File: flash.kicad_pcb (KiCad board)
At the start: 2 copper layers, 17.8 x 27.9 mm, 14 parts, among them J1 USB_B_Micro, J2 Conn_01x05, Q1 PN2222A, Q2 PN2222A, U1 CP2102N-A01-GQFN24

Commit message: Finish PCB
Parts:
- U1: footprint digikey-footprints:QFN-24-1EP_4x4mm -> Housings_DFN_QFN:QFN-24-1EP_4x4mm_Pitch0.5mm
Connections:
- R1 pad 1: Net-(R1-Pad1) -> Net-(C1-Pad1)
- U1 pad 5: Net-(R1-Pad1) -> Net-(C1-Pad1)
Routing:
- net Net-(C1-Pad1): track 7.98 -> 25.9 mm, vias 0 -> 2
- net Net-(R1-Pad1): track 16.7 -> 0.00 mm, vias 2 -> 0
- net GND: track 26.6 -> 30.4 mm, vias 5 -> 6
- net Net-(J1-Pad3): track 16.0 -> 15.3 mm
- net Net-(J1-Pad2): track 14.8 -> 14.2 mm
- net Net-(Q1-Pad1): track 16.0 -> 15.4 mm
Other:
- board text added: "v0.1"

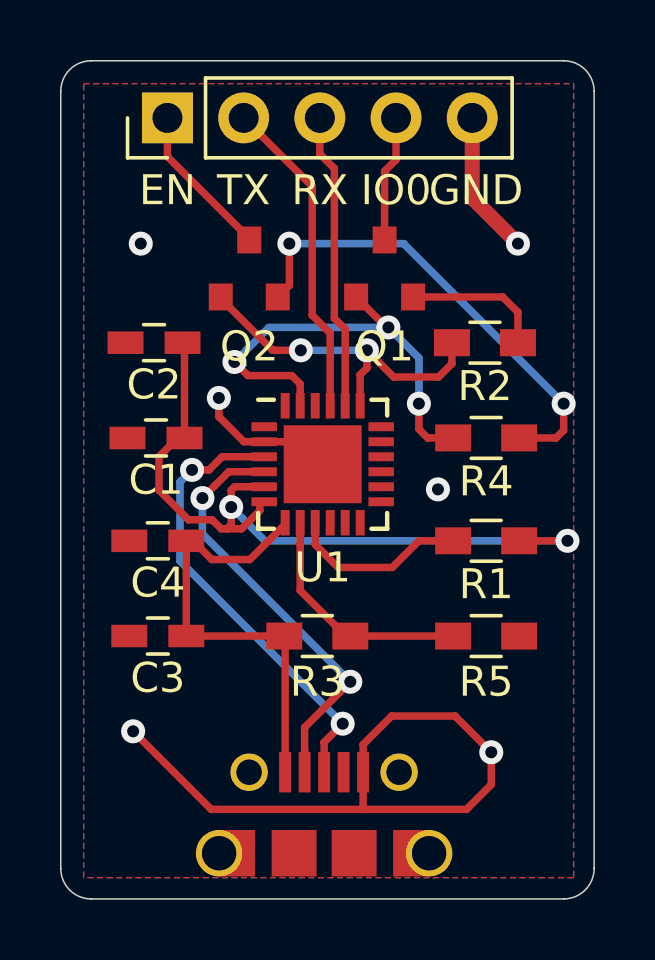
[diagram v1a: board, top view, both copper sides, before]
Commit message: Swap RX/TX pins, fix DTR/RTS transistor wiring
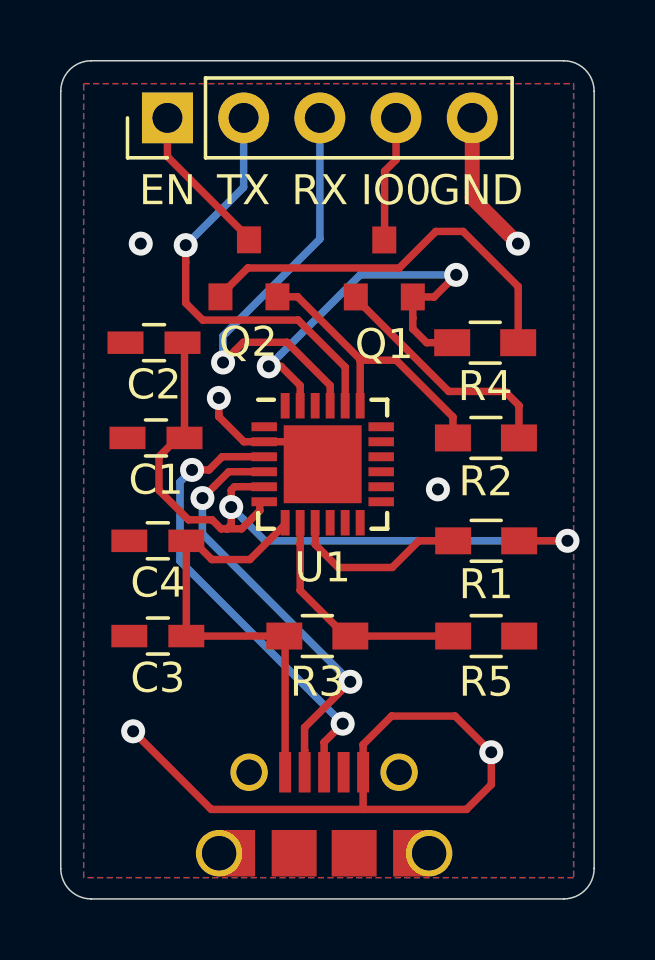
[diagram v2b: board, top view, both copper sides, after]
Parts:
- Q1, Q2: value PN2222A -> MMBT2222ALT1G
- moved R2 3.18 mm to (147.4, 83.6)
- moved R4 3.18 mm to (147.4, 80.4)
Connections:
- J2 pad 2: /TX -> /RX
- J2 pad 3: /RX -> /TX
- Q1 pad 2: Net-(Q1-Pad2) -> /DTR
- Q2 pad 2: Net-(Q2-Pad2) -> /RTS
- R2 pad 1: Net-(Q1-Pad2) -> Net-(Q1-Pad1)
- R2 pad 2: Net-(Q2-Pad1) -> /RTS
- R4 pad 1: Net-(Q2-Pad2) -> Net-(Q2-Pad1)
- R4 pad 2: Net-(Q1-Pad1) -> /DTR
- U1 pad 19: Net-(Q2-Pad1) -> /RTS
- U1 pad 23: Net-(Q1-Pad1) -> /DTR
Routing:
- net Net-(Q2-Pad2): track 15.8 -> 0.00 mm, vias 2 -> 0
- net /DTR: track 0.00 -> 14.2 mm, vias 0 -> 2
- net /RTS: track 0.00 -> 10.0 mm
- net Net-(Q1-Pad1): track 15.4 -> 8.05 mm, vias 3 -> 0
- net Net-(Q1-Pad2): track 4.72 -> 0.00 mm
- net /RX: track 9.90 -> 14.5 mm, vias 0 -> 1
- net /TX: track 10.7 -> 14.6 mm, vias 0 -> 1
- net Net-(Q2-Pad1): track 11.9 -> 13.5 mm, vias 2 -> 0
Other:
- board text added: "v0.2"
- board text removed: "v0.1"
